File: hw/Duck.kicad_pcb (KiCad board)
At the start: 2 copper layers, 33.1 x 16.3 mm, 41 parts, among them J1 Conn_01x06, J2 Conn_01x06, J3 USB_C_Receptacle_USB2.0_14P, Q1 MMBT3904, Q2 MMBT3904, U1 ESP32-S3-PICO-1, U2 SPX3819M5-L-3-3, U3 INMP441, U4 MAX17048G+T10, U5 CH343P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

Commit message: hw: Schematic page layout
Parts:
- J1: value Conn_01x06 -> FFC P0.5
- J2: value Conn_01x06 -> Pin P2.54
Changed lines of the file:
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@@
       )
     )
-    (fp_text value "Conn_01x06" (at 0 15.03) (layer "F.Fab")
+    (fp_text value "Pin P2.54" (at 0 15.03) (layer "F.Fab")
         (effects (font (size 1 1) (thickness 0.15)))
     )
@@
         (effects (font (size 1 1) (thickness 0.1)))
     )
-    (fp_text value "Conn_01x06" (at 0 1 90 unlocked) (layer "F.Fab")
+    (fp_text value "FFC P0.5" (at 0 1 90 unlocked) (layer "F.Fab")
         (effects (font (size 1 1) (thickness 0.15)))
     )

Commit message: hw: Final stretch; submit for fab (Rev. 2)
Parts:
- moved AE1 7.00 mm to (73.3, 56.2)
- moved BT1 7.00 mm to (62.1, 51.8)
- moved C1 7.00 mm to (73.1, 54.5)
- moved C2 7.00 mm to (72.2, 54.5)
- moved C3 7.00 mm to (72.2, 52.6)
- moved C4 7.00 mm to (59.7, 52.9)
- moved C5 7.00 mm to (59.7, 54.8)
- moved C6 7.00 mm to (72.9, 53.9)
- moved C7 7.00 mm to (64.3, 54.1)
- moved D1 7.00 mm to (61.8, 49.6)
- moved G*** 7.00 mm to (71.8, 59.3)
- moved J1 7.00 mm to (73.2, 50.1)
- moved R1 7.00 mm to (73.2, 52.6)
- moved R2 7.00 mm to (65.7, 50.5)
- moved R3 7.00 mm to (66.2, 51.5)
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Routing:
- net /U0TXD: track 31.6 -> 38.9 mm
- net +3V3: track 58.8 -> 51.6 mm
- net /ESP_EN: track 31.9 -> 25.5 mm
- net /U0RXD: track 26.3 -> 31.7 mm
- net /BOOT0: track 19.4 -> 20.7 mm
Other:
- board size 33.1 x 16.3 mm -> 33.1 x 22.7 mm

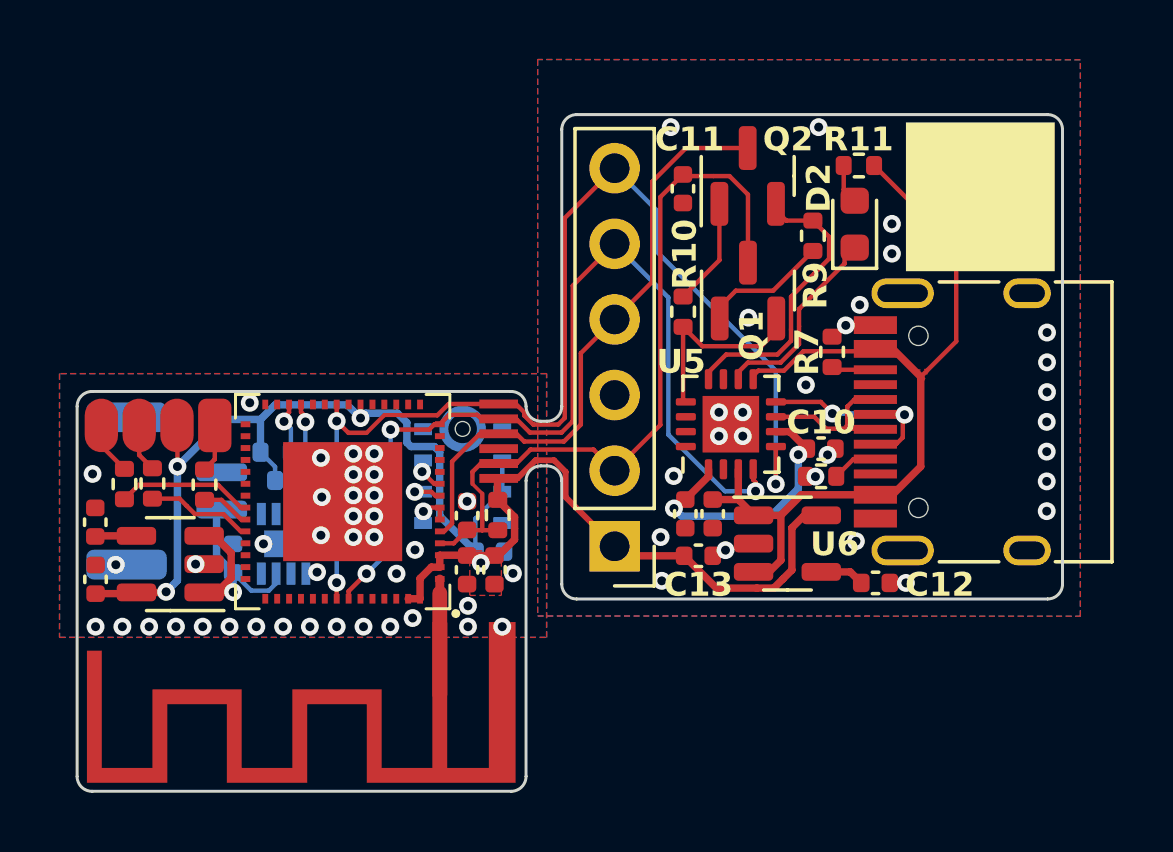
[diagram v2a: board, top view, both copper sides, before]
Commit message: hw: Revise schematic and update PCB; resubmit (Rev. 2)
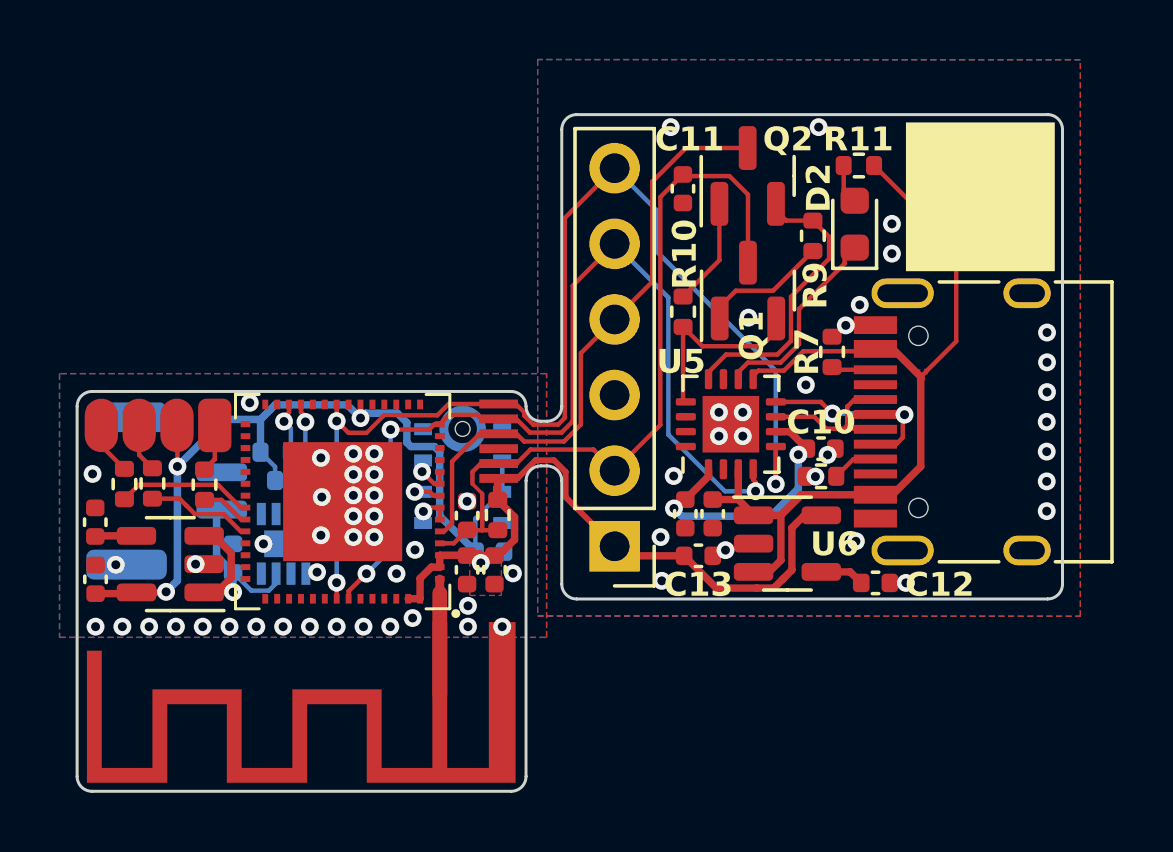
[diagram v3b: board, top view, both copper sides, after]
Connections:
- U1 pad 10: unconnected-(U1-GPIO5-Pad10) -> /MIC_WS

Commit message: hw: Fix missing power line (/_<); resubmit (Rev. 2)
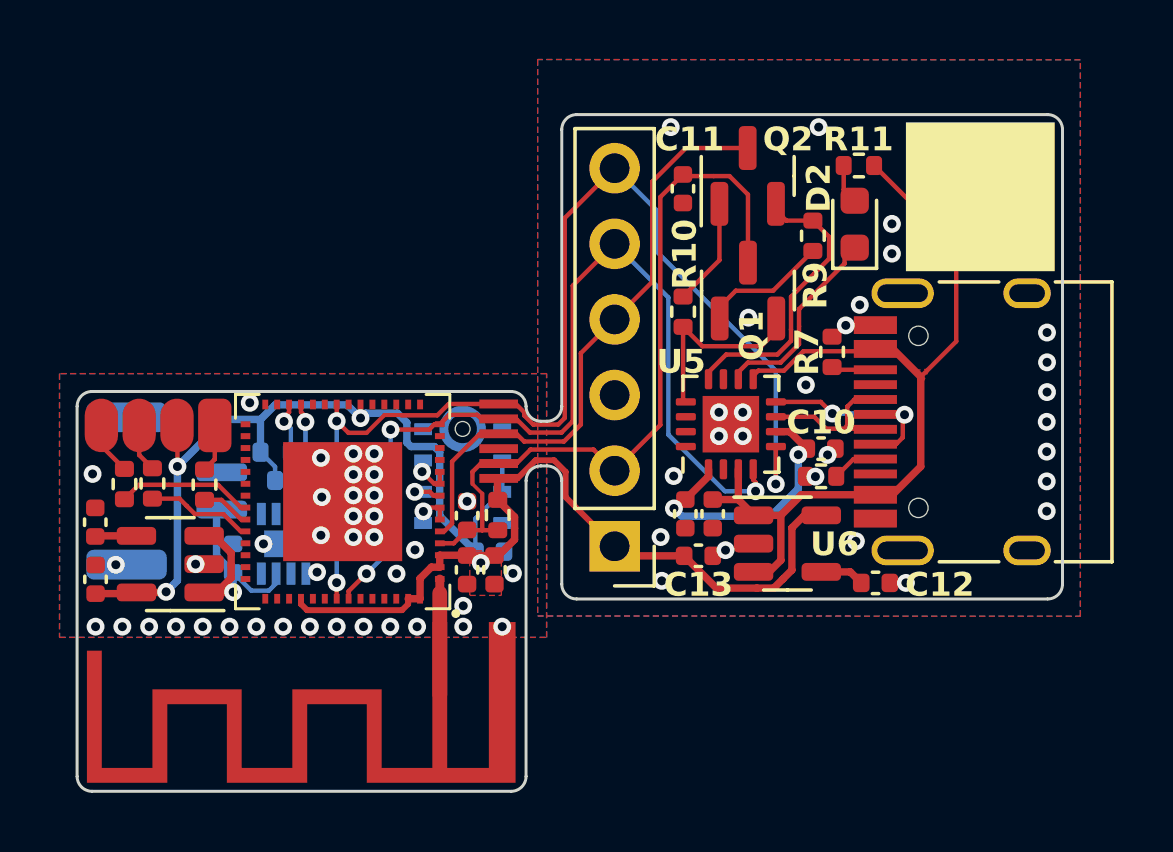
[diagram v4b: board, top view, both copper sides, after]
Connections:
- U1 pad 46: unconnected-(U1-VDD_CPU-Pad46) -> +3V3
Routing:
- net +3V3: track 51.6 -> 55.7 mm
